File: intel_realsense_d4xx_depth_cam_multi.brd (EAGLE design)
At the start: 37.4 x 22.8 mm, 6 parts, among them SW1 300mA/4V

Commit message: Rev 1: Board complete.
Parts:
- added U$4, U$5: (no value), PiB_logo:MRSWIRLYEYES-LOGO
- renumbered U$1 to CAM1, U$2 to CAM2, U$3 to CAM3
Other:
- board size 37.4 x 22.8 mm -> 37.4 x 21.3 mm
- board text added: "Designed by:"
- board text added: "Intel Realsense D4XX Multi (3x) Depth CAM"
- board text added: "MrSwirlyEyes"
- board text added: "OFF"
- board text added: "ON"
- board text added: "Rev 1"
- board text added: "mrswirlyeyes.com"
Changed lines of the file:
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@@
 </layers>
 <board>
+<fusionsync huburn="a.cGVyc29uYWw6dWUyOTIwMzJm" projecturn="a.cGVyc29uYWw6dWUyOTIwMzJmIzIwMTYwNDI5MzA4MDY3NTY" f3durn="urn:adsk.wipprod:dm.lineage:O28O6C-qS_GBEwGM4ZqODw" pcbguid="62f0b917-b0ba-40be-aa7b-2ff664897ed8" lastpulledtime="" lastsyncedchangeguid="0cc64ee9-2472-b7ca-e1b6-31f0371193c6"/>
 <plain>
-<wire x1="-18.7" y1="0" x2="18.7" y2="0" width="0" layer="20"/>
-<wire x1="18.7" y1="0" x2="18.7" y2="22.8" width="0" layer="20"/>
+<wire x1="-18.7" y1="1.5" x2="18.7" y2="1.5" width="0" layer="20"/>
+<wire x1="18.7" y1="1.5" x2="18.7" y2="22.8" width="0" layer="20"/>
 <wire x1="18.7" y1="22.8" x2="-18.7" y2="22.8" width="0" layer="20"/>
-<wire x1="-18.7" y1="22.8" x2="-18.7" y2="0" width="0" layer="20"/>
+<wire x1="-18.7" y1="22.8" x2="-18.7" y2="1.5" width="0" layer="20"/>
+<text x="9" y="10" size="1" layer="21" font="vector" ratio="10" align="top-left">Rev 1</text>
+<text x="-18" y="22" size="0.5" layer="21" font="vector" ratio="10" align="top-left">Designed by:</text>
+<text x="-17" y="21" size="1" layer="21" font="vector" ratio="15" align="top-left">MrSwirlyEyes</text>
+<text x="7.8" y="22.3" size="1" layer="21" font="vector" ratio="15" align="top-left">Intel Realsense
+D4XX Multi (3x)
+Depth CAM</text>
+<text x="0" y="22" size="1" layer="22" font="vector" ratio="15" rot="MR0" align="top-center">mrswirlyeyes.com</text>
+<text x="-9" y="21" size="1" layer="22" font="vector" ratio="15" rot="MR0" align="top-left">MrSwirlyEyes</text>
+<text x="-9" y="22" size="0.5" layer="22" font="vector" ratio="10" rot="MR0" align="top-left">Designed by:</text>
+<text x="18" y="22.3" size="1" layer="22" font="vector" ratio="15" rot="MR0" align="top-left">Intel Realsense
+D4XX Multi (3x)
+Depth CAM</text>
+<text x="18.2" y="9.6" size="0.75" layer="21" font="vector" ratio="10" align="top-right">ON</text>
+<text x="18.2" y="18.4" size="0.75" layer="21" font="vector" ratio="10" align="bottom-right">OFF</text>
 </plain>
 <attributes>
@@
 </autorouter>
 <elements>
-<element name="U$1" library="PiB_connectors" library_urn="urn:adsk.eagle:library:6338520" package="SM09B-SRSS-TB" package3d_urn="urn:adsk.eagle:package:6338575/1" value="SM09B-SRSS-TB" x="-12.4" y="4.3" smashed="yes">
+<element name="CAM1" library="PiB_connectors" library_urn="urn:adsk.eagle:library:6338520" package="SM09B-SRSS-TB" package3d_urn="urn:adsk.eagle:package:6338575/1" value="SM09B-SRSS-TB" x="-12.4" y="4.3" smashed="yes">
 <attribute name="DATASHEET" value="http://www.jst-mfg.com/product/pdf/eng/eSH.pdf" x="6.65" y="-0.78" size="1.778" layer="27" display="off"/>
 <attribute name="DATASHEET_HOUSING" value="http://www.jst-mfg.com/product/pdf/eng/eSH.pdf" x="6.65" y="-0.78" size="1.778" layer="27" display="off"/>
@@
 <attribute name="VALUE" x="-12.4" y="3.3" size="0.25" layer="27" font="vector" ratio="10" align="center"/>
 </element>
-<element name="U$2" library="PiB_connectors" library_urn="urn:adsk.eagle:library:6338520" package="SM09B-SRSS-TB" package3d_urn="urn:adsk.eagle:package:6338575/1" value="SM09B-SRSS-TB" x="0" y="4.3" smashed="yes">
+<element name="CAM2" library="PiB_connectors" library_urn="urn:adsk.eagle:library:6338520" package="SM09B-SRSS-TB" package3d_urn="urn:adsk.eagle:package:6338575/1" value="SM09B-SRSS-TB" x="0" y="4.3" smashed="yes">
 <attribute name="DATASHEET" value="http://www.jst-mfg.com/product/pdf/eng/eSH.pdf" x="19.05" y="-9.67" size="1.778" layer="27" display="off"/>
 <attribute name="DATASHEET_HOUSING" value="http://www.jst-mfg.com/product/pdf/eng/eSH.pdf" x="19.05" y="-9.67" size="1.778" layer="27" display="off"/>
@@
 <attribute name="VALUE" x="0" y="3.3" size="0.25" layer="27" font="vector" ratio="10" align="center"/>
 </element>
-<element name="U$3" library="PiB_connectors" library_urn="urn:adsk.eagle:library:6338520" package="SM09B-SRSS-TB" package3d_urn="urn:adsk.eagle:package:6338575/1" value="SM09B-SRSS-TB" x="12.4" y="4.3" smashed="yes">
+<element name="CAM3" library="PiB_connectors" library_urn="urn:adsk.eagle:library:6338520" package="SM09B-SRSS-TB" package3d_urn="urn:adsk.eagle:package:6338575/1" value="SM09B-SRSS-TB" x="12.4" y="4.3" smashed="yes">
 <attribute name="DATASHEET" value="http://www.jst-mfg.com/product/pdf/eng/eSH.pdf" x="31.45" y="-18.56" size="1.778" layer="27" display="off"/>
 <attribute name="DATASHEET_HOUSING" value="http://www.jst-mfg.com/product/pdf/eng/eSH.pdf" x="31.45" y="-18.56" size="1.778" layer="27" display="off"/>
@@
 <attribute name="VALUE" x="13.7" y="14" size="0.5" layer="27" font="vector" ratio="10" rot="R90" align="top-center"/>
 </element>
+<element name="U$4" library="PiB_logo" package="MRSWIRLYEYES-LOGO" value="" x="-13" y="14" smashed="yes" rot="MR0"/>
+<element name="U$5" library="PiB_logo" package="MRSWIRLYEYES-LOGO" value="" x="-13" y="14" smashed="yes"/>
 </elements>
 <signals>
 <signal name="GND">
-<contactref element="U$1" pad="9"/>
-<contactref element="U$3" pad="9"/>
-<contactref element="U$2" pad="9"/>
+<contactref element="CAM1" pad="9"/>
+<contactref element="CAM3" pad="9"/>
+<contactref element="CAM2" pad="9"/>
 <contactref element="BNC1" pad="-"/>
 <polygon width="0.1524" layer="16">
 <vertex x="-18.7" y="22.8"/>
-<vertex x="-18.7" y="0"/>
-<vertex x="18.7" y="0"/>
+<vertex x="-18.7" y="1.5"/>
+<vertex x="18.7" y="1.5"/>
 <vertex x="18.7" y="22.8"/>
 </polygon>
 <polygon width="0.1524" layer="1">
 <vertex x="-18.7" y="22.8"/>
-<vertex x="-18.7" y="0"/>
-<vertex x="18.7" y="0"/>
+<vertex x="-18.7" y="1.5"/>
+<vertex x="18.7" y="1.5"/>
 <vertex x="18.7" y="22.8"/>
 </polygon>
@@
 </signal>
 <signal name="SYNC">
-<contactref element="U$3" pad="5"/>
-<contactref element="U$2" pad="5"/>
-<contactref element="U$1" pad="5"/>
+<contactref element="CAM3" pad="5"/>
+<contactref element="CAM2" pad="5"/>
+<contactref element="CAM1" pad="5"/>
 <wire x1="-12.4" y1="6.75" x2="-12.4" y2="5.7" width="0.381" layer="1"/>
 <wire x1="-12.4" y1="5.7" x2="-11.7" y2="5" width="0.381" layer="1"/>
@@
 </signals>
 <mfgpreviewcolors>
-<mfgpreviewcolor name="soldermaskcolor" color="0xC8008000"/>
+<mfgpreviewcolor name="soldermaskcolor" color="0xC855007F"/>
 <mfgpreviewcolor name="silkscreencolor" color="0xFFFEFEFE"/>
 <mfgpreviewcolor name="backgroundcolor" color="0xFF282828"/>
@@
 </drawing>
 <compatibility>
+<note version="6.3" minversion="6.2.2" severity="warning">
+Since Version 6.2.2 text objects can contain more than one line,
+which will not be processed correctly with this version.
+</note>
 <note version="8.2" severity="warning">
 Since Version 8.2, EAGLE supports online libraries. The ids
@@
 </note>
 <note version="8.3" severity="warning">
+Since Version 8.3, EAGLE supports Fusion synchronisation.
+This feature will not be available in this version and saving
+the document will break the link to the Fusion PCB feature.
+</note>
+<note version="8.3" severity="warning">

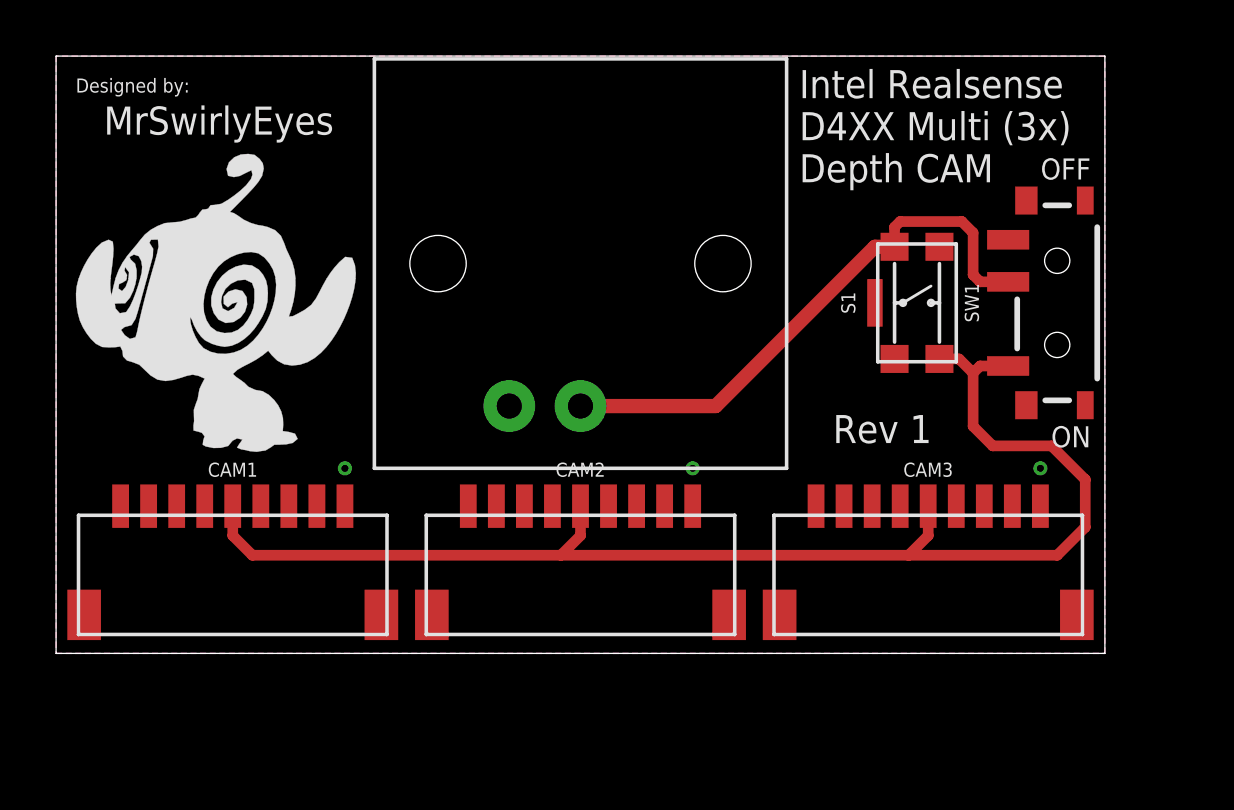
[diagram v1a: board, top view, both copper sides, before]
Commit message: Add 22nF cap and 20K resistor.
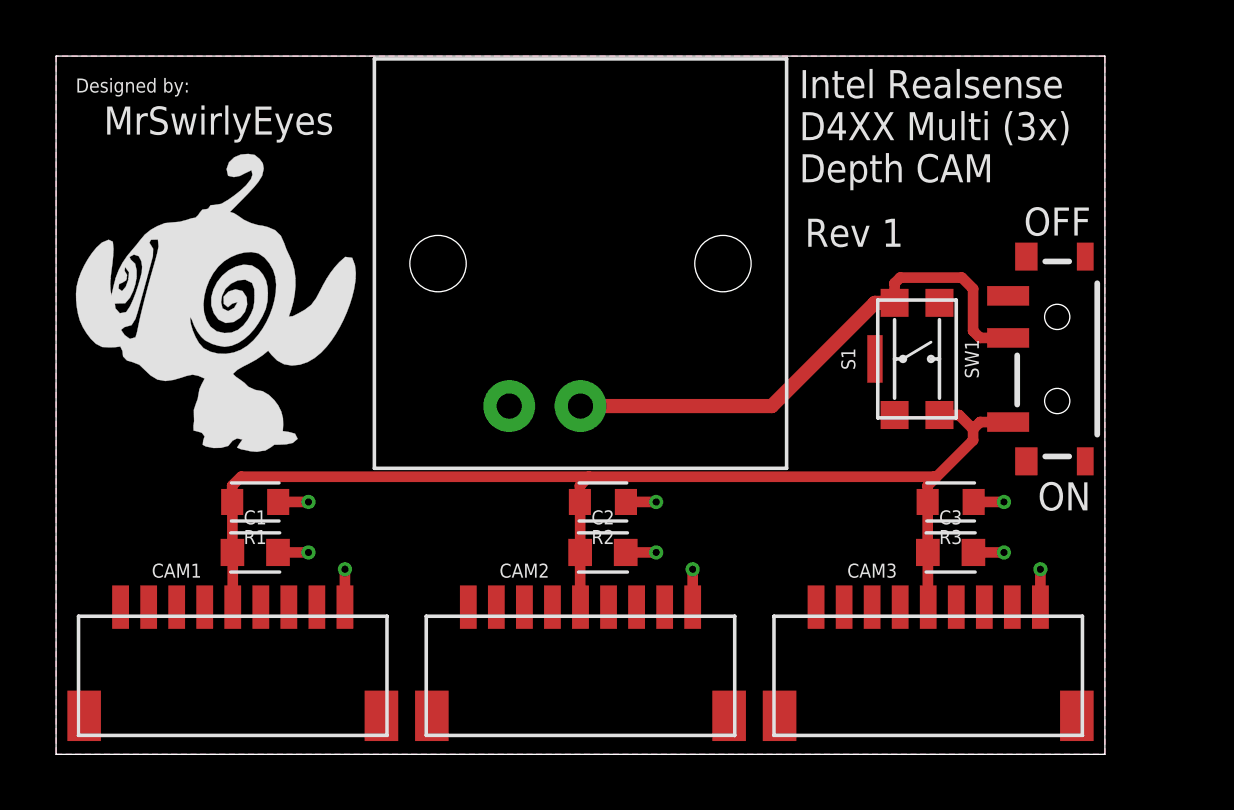
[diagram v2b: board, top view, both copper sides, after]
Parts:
- added C1, C2, C3: 20nF/50V, PiB_capacitors:CAPC1608X95
- added R1, R2, R3: 20K, PiB_resistors:RESC1608X65_SMD-0603
- moved CAM1 3.60 mm to (-12.4, 0.70)
- moved CAM2 3.60 mm to (0.00, 0.70)
- moved CAM3 3.60 mm to (12.4, 0.70)
- moved S1 2.00 mm to (12.0, 12.0)
- moved SW1 2.00 mm to (17.0, 12.0)
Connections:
- net GND: now also C1.2, C2.2, C3.2, R1.1, R2.1, R3.1
- net SYNC: now also C1.1, C2.1, C3.1, R1.2, R2.2, R3.2
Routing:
- net GND: track 0.00 -> 10.6 mm, vias 3 -> 9
- net SYNC: track 47.4 -> 44.1 mm
- net N$1: track 20.2 -> 19.3 mm
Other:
- board size 37.4 x 21.3 mm -> 37.4 x 24.9 mm

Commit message: Add BOM for intel depth cam.
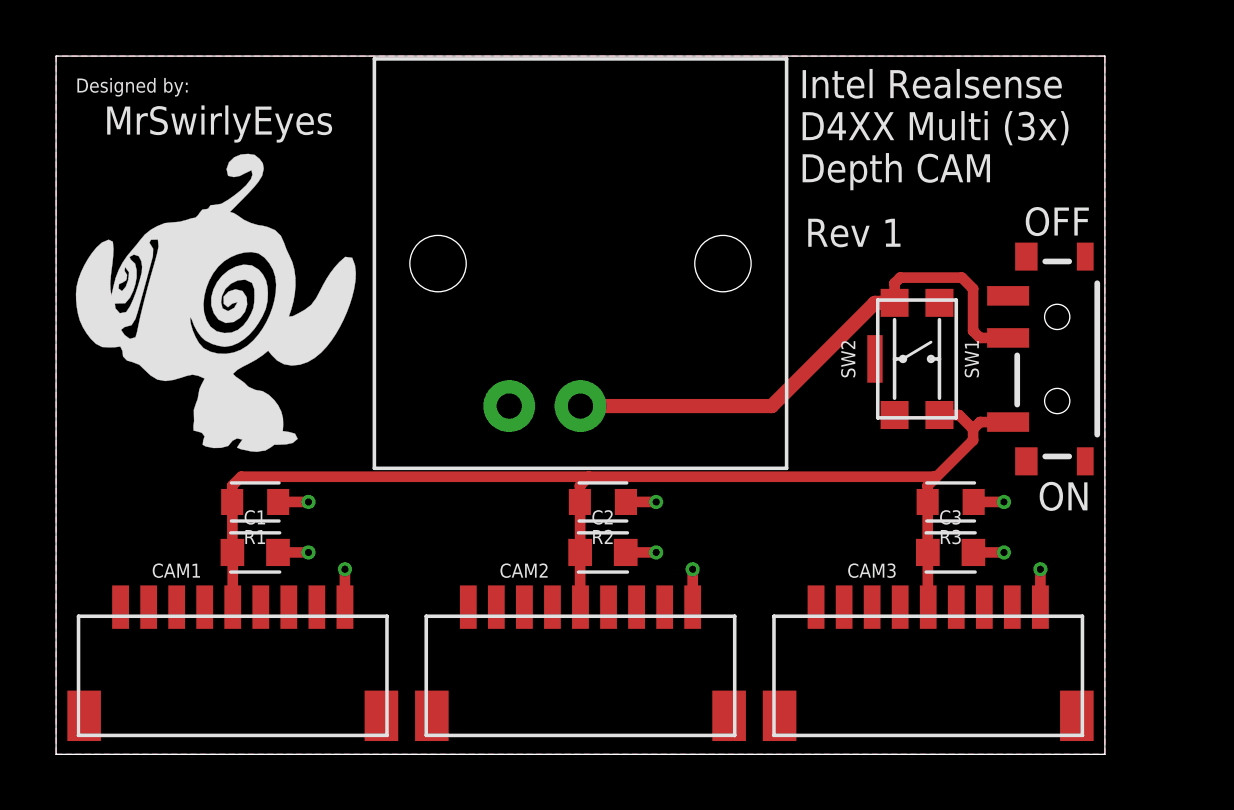
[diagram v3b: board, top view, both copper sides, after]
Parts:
- BNC1: value BNC 50OHM 4GHz -> BNC 75OHM 2GHz
- renumbered S1 to SW2
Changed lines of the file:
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@@
 </layers>
 <board>
-<fusionsync huburn="a.cGVyc29uYWw6dWUyOTIwMzJm" projecturn="a.cGVyc29uYWw6dWUyOTIwMzJmIzIwMTYwNDI5MzA4MDY3NTY" f3durn="urn:adsk.wipprod:dm.lineage:O28O6C-qS_GBEwGM4ZqODw" pcbguid="62f0b917-b0ba-40be-aa7b-2ff664897ed8" lastpulledtime="" lastsyncedchangeguid="8800b89f-20c9-5480-1314-b8252c44279b"/>
+<fusionsync huburn="a.cGVyc29uYWw6dWUyOTIwMzJm" projecturn="a.cGVyc29uYWw6dWUyOTIwMzJmIzIwMTYwNDI5MzA4MDY3NTY" f3durn="urn:adsk.wipprod:dm.lineage:O28O6C-qS_GBEwGM4ZqODw" pcbguid="62f0b917-b0ba-40be-aa7b-2ff664897ed8" lastpulledtime="" lastsyncedchangeguid="9aca7025-9b01-9632-26e4-a0b3e293ce1b"/>
 <plain>
 <wire x1="-18.7" y1="-2.1" x2="18.7" y2="-2.1" width="0" layer="20"/>
@@
 <attribute name="VALUE" x="12.4" y="-0.3" size="0.25" layer="27" font="vector" ratio="10" align="center"/>
 </element>
-<element name="BNC1" library="PiB_connectors" package="BNC_RA_1-1337543-0" package3d_urn="urn:adsk.eagle:package:6338576/2" value="BNC 50OHM 4GHz" x="0" y="15.4" smashed="yes">
-<attribute name="DATASHEET" value="https://www.te.com/commerce/DocumentDelivery/DDEController?Action=srchrtrv&amp;DocNm=1337543&amp;DocType=Customer+Drawing&amp;DocLang=English" x="0" y="15.4" size="1.778" layer="27" display="off"/>
+<element name="BNC1" library="PiB_connectors" package="BNC_RA_1-1337543-0" package3d_urn="urn:adsk.eagle:package:6338576/2" value="BNC 75OHM 2GHz" x="0" y="15.4" smashed="yes">
+<attribute name="DATASHEET" value="https://www.te.com/commerce/DocumentDelivery/DDEController?Action=srchrtrv&amp;DocNm=1478032&amp;DocType=Customer+Drawing&amp;DocLang=English" x="0" y="15.4" size="1.778" layer="27" display="off"/>
 <attribute name="DIST" value="Digikey" x="0" y="15.4" size="1.778" layer="27" display="off"/>
-<attribute name="DISTLINK" value="https://www.digikey.com/products/en?keywords=A97553-ND" x="0" y="15.4" size="1.778" layer="27" display="off"/>
-<attribute name="DISTPN" value="A97553-ND" x="0" y="15.4" size="1.778" layer="27" display="off"/>
+<attribute name="DISTLINK" value="https://www.digikey.com/products/en?keywords=A97560-ND" x="0" y="15.4" size="1.778" layer="27" display="off"/>
+<attribute name="DISTPN" value="A97560-ND" x="0" y="15.4" size="1.778" layer="27" display="off"/>
 <attribute name="MFR" value="TE Connectivity AMP Connectors" x="0" y="15.4" size="1.778" layer="27" display="off"/>
-<attribute name="MPN" value="1-1337543-0" x="0" y="15.4" size="1.778" layer="27" display="off"/>
+<attribute name="MPN" value="1-1478032-0" x="0" y="15.4" size="1.778" layer="27" display="off"/>
 </element>
 <element name="SW1" library="PiB_switches" package="SW_SLIDE_SPDT_RA_SMD_4V_300MA_6.7L-2.6W" package3d_urn="urn:adsk.eagle:package:2959400/3" value="300mA/4V" x="17" y="12" smashed="yes" rot="R180">
@@
 <attribute name="VALUE" x="18.143" y="12" size="0.25" layer="27" font="vector" ratio="10" rot="R270" align="top-center"/>
 </element>
-<element name="S1" library="PiB_switches" package="BTN_MOMENTARY_SPDT-NO_L4.6-W2.8" package3d_urn="urn:adsk.eagle:package:3034784/2" value="50mA/32V" x="12" y="12" smashed="yes" rot="R90">
+<element name="SW2" library="PiB_switches" package="BTN_MOMENTARY_SPDT-NO_L4.6-W2.8" package3d_urn="urn:adsk.eagle:package:3034784/2" value="50mA/32V" x="12" y="12" smashed="yes" rot="R90">
 <attribute name="DATASHEET" value="https://www.ckswitches.com/media/1479/kmr2.pdf" x="12" y="12" size="1.778" layer="27" rot="R90" display="off"/>
 <attribute name="DIST" value="Digikey" x="12" y="12" size="1.778" layer="27" rot="R90" display="off"/>
@@
 <wire x1="14.25" y1="9.75" x2="14" y2="9.5" width="0.381" layer="1"/>
 <wire x1="14" y1="9.1" x2="14" y2="9.5" width="0.381" layer="1"/>
-<contactref element="S1" pad="3"/>
+<contactref element="SW2" pad="3"/>
 <wire x1="12.8" y1="10" x2="13.5" y2="10" width="0.381" layer="1"/>
 <wire x1="13.5" y1="10" x2="14" y2="9.5" width="0.381" layer="1"/>
@@
 <contactref element="BNC1" pad="+"/>
 <contactref element="SW1" pad="2"/>
-<contactref element="S1" pad="2"/>
+<contactref element="SW2" pad="2"/>
 <wire x1="15.25" y1="12.75" x2="14.25" y2="12.75" width="0.381" layer="1"/>
 <wire x1="14.25" y1="12.75" x2="14" y2="13" width="0.381" layer="1"/>
